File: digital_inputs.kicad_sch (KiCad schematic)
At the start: 11 parts, among them J2 Samtec Isorate, J3 Samtec Isorate, U8 SN74LVC16244A-EP

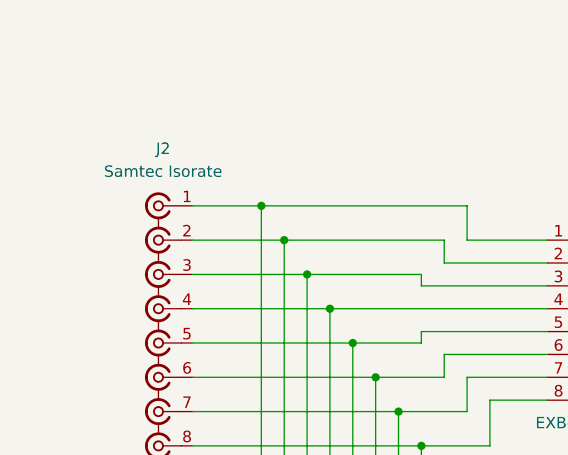
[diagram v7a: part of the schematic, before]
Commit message: Updated Footprint of Connectors
-Added a 0 ohm resistor after the 5V LDO
- fixed some part numbers
- adding 3d model to the isorate connectors
- updated datasheet/design docs
- changed one of the DIO connector to a vertical connector
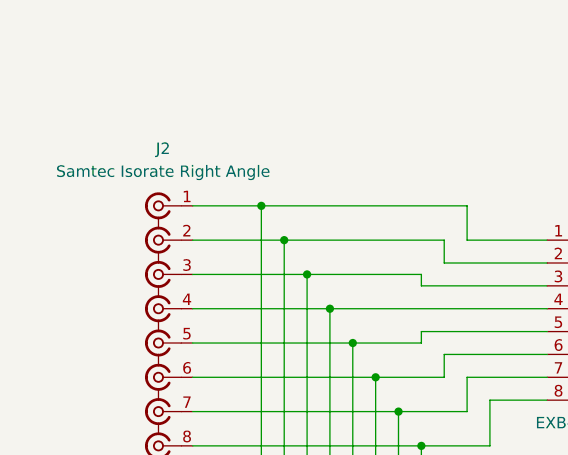
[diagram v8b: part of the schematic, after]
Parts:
- J2: value Samtec Isorate -> Samtec Isorate Right Angle
- J3: footprint rf-input-fmc:SAMTEC_IP5-08-01-L-S-RA1-L-TR -> rf-input-fmc:SAMTEC_IP5-08-05.0-L-S-1-L-TR; MPN SAMTEC_IP5-08-01-L-S-RA1-L-TR -> SAMTEC_IP5-08-05.0-L-S-1-L-TR
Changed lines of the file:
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@@
 			)
 		)
-		(property "Footprint" "rf-input-fmc:SAMTEC_IP5-08-01-L-S-RA1-L-TR"
+		(property "Footprint" "rf-input-fmc:SAMTEC_IP5-08-05.0-L-S-1-L-TR"
 			(at 44.45 113.03 0)
 			(effects
@@
 			)
 		)
-		(property "MPN" "SAMTEC_IP5-08-01-L-S-RA1-L-TR"
+		(property "MPN" "SAMTEC_IP5-08-05.0-L-S-1-L-TR"
 			(at 44.45 113.03 0)
 			(effects
@@
 			)
 		)
-		(property "Value" "Samtec Isorate"
+		(property "Value" "Samtec Isorate Right Angle"
 			(at 44.9696 53.34 0)
 			(effects
